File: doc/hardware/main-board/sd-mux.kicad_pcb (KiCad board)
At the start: 2 copper layers, 50 x 132 mm, 54 parts, among them J1 SDCARD, P1 USB_OTG, P10 MKDS 1,5/3, P2 629105136821, P3 61400416021, P4 61400416021, P5 IDC_02X04, P6 IDC_02X04, P7 MKDS 1,5/3, Q1 IRF7606PBF, Q2 IRF7606PBF, Q3 IRF7606PBF, Q4 IRF7606PBF, Q5 2N7002, Q6 2N7002, Q7 IRF7606PBF, Q8 IRF7606PBF, U1 TS3USB30EDGSR, U2 FT245RL, U3 74AHC1G14, U4 TS3A27518E, U5 74AHC1G14

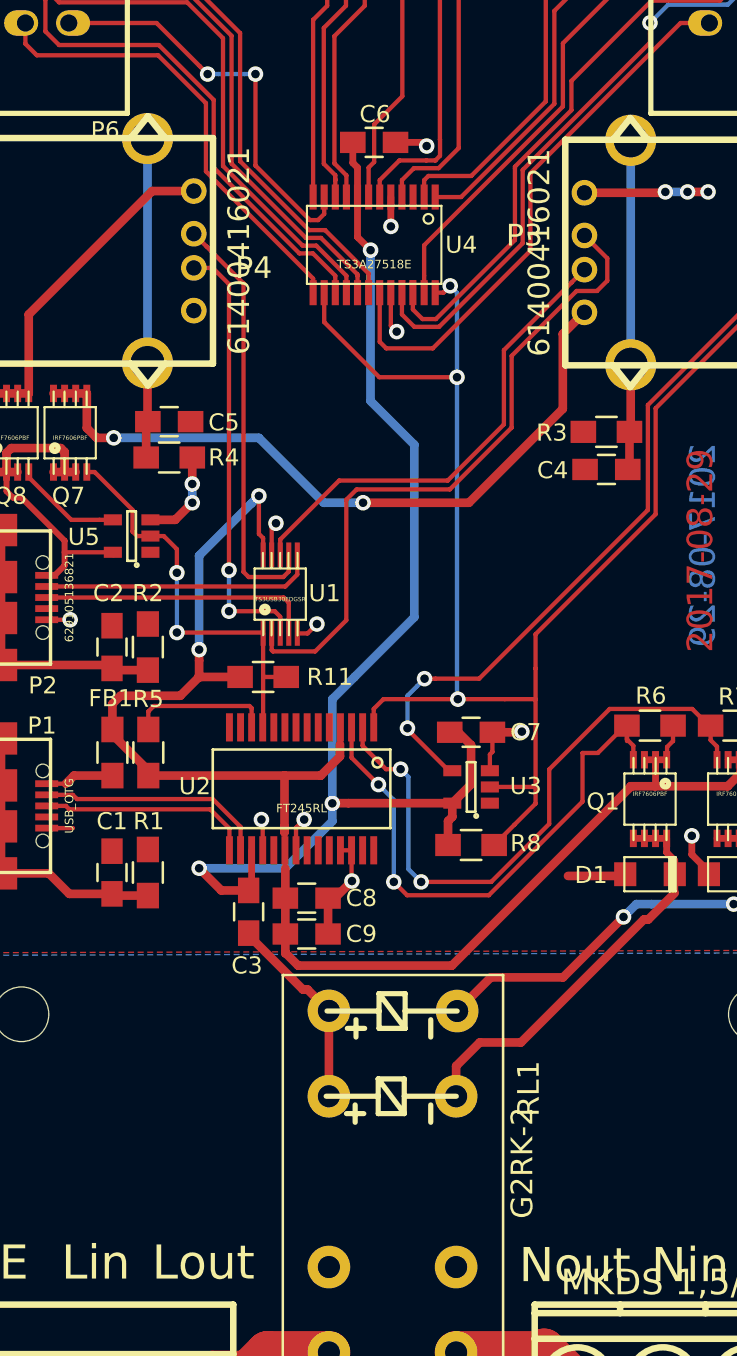
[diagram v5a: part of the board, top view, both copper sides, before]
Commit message: Fix unrouted tracks
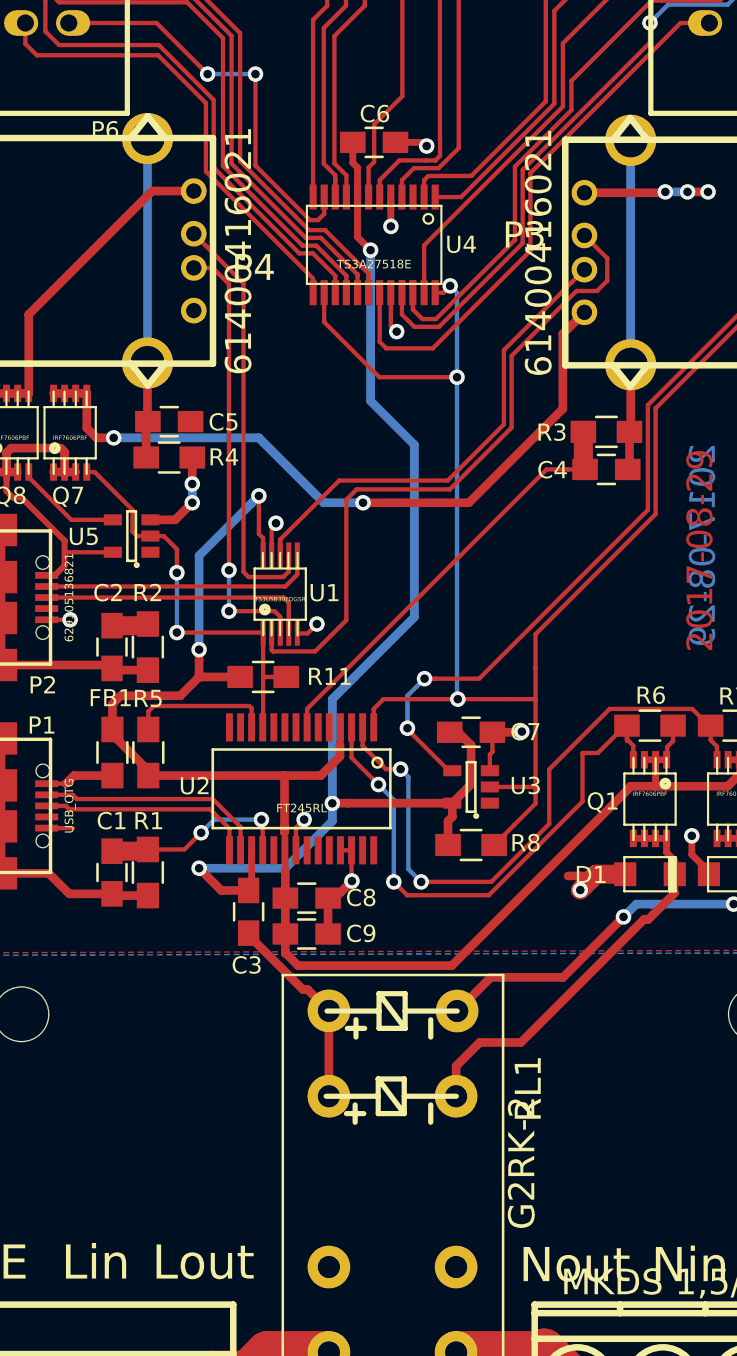
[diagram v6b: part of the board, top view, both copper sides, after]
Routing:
- net GND: track 157.1 -> 197.2 mm, vias 26 -> 28
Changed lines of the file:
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@@
-(kicad_pcb (version 4) (host pcbnew 4.0.5)
+(kicad_pcb (version 20171130) (host pcbnew "(5.0.0-rc2-dev-707-g2ed24a4)")
   (general
-    (links 171)
-    (no_connects 0)
-    (area 118.124519 15.525479 168.274521 147.675481)
     (thickness 1.6)
     (drawings 19)
-    (tracks 731)
+    (tracks 749)
     (zones 0)
     (modules 54)
@@
   )
   (setup
-    (last_trace_width 0.254)
+    (last_trace_width 1.116)
     (user_trace_width 0.508)
     (user_trace_width 1.116)
@@
       (layerselection 0x010fc_80000001)
       (usegerberextensions true)
+      (usegerberattributes false)
+      (usegerberadvancedattributes false)
+      (creategerberjobfile false)
       (excludeedgelayer false)
       (linewidth 0.100000)
@@
       (hpglpenspeed 20)
       (hpglpendiameter 15)
-      (hpglpenoverlay 2)
       (psnegative false)
       (psa4output false)
@@
     (tags SOT-23-5)
     (attr smd)
-    (fp_text reference U3 (at -3.2 0.05 360) (layer F.SilkS)
+    (fp_text reference U3 (at -3.2 0.05) (layer F.SilkS)
       (effects (font (size 1 1) (thickness 0.15)))
     )
@@
     (at 131.13626 43.545748 270)
     (descr MSOIC-8)
-    (fp_text reference Q3 (at 2.354732 -0.06326 360) (layer F.SilkS)
+    (fp_text reference Q3 (at 2.354732 -0.06326) (layer F.SilkS)
       (effects (font (size 1 1) (thickness 0.15)))
     )
@@
     (tags "capacitor 0805")
     (attr smd)
-    (fp_text reference C3 (at 3.15 0.1 360) (layer F.SilkS)
+    (fp_text reference C3 (at 3.15 0.1) (layer F.SilkS)
       (effects (font (size 1 1) (thickness 0.15)))
     )
@@
     (tags "capacitor 0805")
     (attr smd)
-    (fp_text reference C4 (at 3.15 -0.05 360) (layer F.SilkS)
+    (fp_text reference C4 (at 3.15 -0.05) (layer F.SilkS)
       (effects (font (size 1 1) (thickness 0.15)))
     )
@@
     (tags "resistor 0805")
     (attr smd)
-    (fp_text reference FB1 (at -3.17452 0.10548 360) (layer F.SilkS)
+    (fp_text reference FB1 (at -3.17452 0.10548) (layer F.SilkS)
       (effects (font (size 1 1) (thickness 0.15)))
     )
@@
     (at 120.45 99.85 270)
     (descr "USB B micro")
-    (fp_text reference P1 (at -4.7 -2.4 360) (layer F.SilkS)
+    (fp_text reference P1 (at -4.7 -2.4) (layer F.SilkS)
       (effects (font (size 1 1) (thickness 0.15)))
     )
@@
     (at 120.45 87.65 270)
     (descr "USB B micro")
-    (fp_text reference P2 (at 5.15048 -2.44952 360) (layer F.SilkS)
+    (fp_text reference P2 (at 5.15048 -2.44952) (layer F.SilkS)
       (effects (font (size 1 1) (thickness 0.15)))
     )
@@
     (at 159.19952 133.65048 180)
     (descr "3 Pins 5mm screw connector")
-    (fp_text reference P7 (at 0.2 -6.6 360) (layer F.SilkS)
+    (fp_text reference P7 (at 0.2 -6.6) (layer F.SilkS)
       (effects (font (size 1 1) (thickness 0.25)))
     )
@@
     (tags "resistor 0805")
     (attr smd)
-    (fp_text reference R3 (at 3.2 -0.05 360) (layer F.SilkS)
+    (fp_text reference R3 (at 3.2 -0.05) (layer F.SilkS)
       (effects (font (size 1 1) (thickness 0.15)))
     )
@@
     (descr "relay, V23042-B2 series")
     (fp_text reference RL1 (at -7.95 -7.95 270) (layer F.SilkS)
-      (effects (font (thickness 0.3048)))
+      (effects (font (size 1.524 1.524) (thickness 0.3048)))
     )
     (fp_text value G2RK-2 (at -3.6 -7.57 270) (layer F.SilkS)
-      (effects (font (thickness 0.3048)))
+      (effects (font (size 1.524 1.524) (thickness 0.3048)))
     )
     (fp_line (start 14.6 6.45) (end 14.6 -6.45) (layer F.SilkS) (width 0.15))
@@
     (descr "USB A Socket")
     (fp_text reference P3 (at 1 -9.5 180) (layer F.SilkS)
-      (effects (font (thickness 0.3048)))
+      (effects (font (size 1.524 1.524) (thickness 0.3048)))
     )
     (fp_text value 61400416021 (at 0 -8.636 90) (layer F.SilkS)
-      (effects (font (thickness 0.3048)))
+      (effects (font (size 1.524 1.524) (thickness 0.3048)))
     )
     (fp_line (start -7.62 6.985) (end 7.62 6.985) (layer F.SilkS) (width 0.381))
@@
     (at 125.75 67.35 270)
     (descr "USB A Socket")
-    (fp_text reference P4 (at 1 -9.5 360) (layer F.SilkS)
-      (effects (font (thickness 0.3048)))
+    (fp_text reference P4 (at 1 -9.5) (layer F.SilkS)
+      (effects (font (size 1.524 1.524) (thickness 0.3048)))
     )
     (fp_text value 61400416021 (at 0 -8.636 270) (layer F.SilkS)
-      (effects (font (thickness 0.3048)))
+      (effects (font (size 1.524 1.524) (thickness 0.3048)))
     )
     (fp_line (start -7.62 6.985) (end 7.62 6.985) (layer F.SilkS) (width 0.381))
@@
     (descr "PINS Box 4x2 2.54")
     (tags "CONN DEV")
-    (fp_text reference P6 (at 10.09952 -3.40048 360) (layer F.SilkS)
+    (fp_text reference P6 (at 10.09952 -3.40048) (layer F.SilkS)
       (effects (font (size 1 1) (thickness 0.2032)))
     )
@@
   (segment (start 123.12462 88.95048) (end 124.49952 88.95048) (width 0.254) (layer F.Cu) (net 2))
   (segment (start 124.49952 88.95048) (end 124.5 88.95) (width 0.254) (layer F.Cu) (net 2))
+  (segment (start 153.64504 80.15) (end 154.64904 80.15) (width 0.254) (layer F.Cu) (net 2))
+  (segment (start 152.39644 80.15) (end 153.64504 80.15) (width 0.254) (layer F.Cu) (net 2))
+  (segment (start 138.37512 94.17132) (end 152.39644 80.15) (width 0.254) (layer F.Cu) (net 2))
+  (segment (start 138.37512 95.25082) (end 138.37512 94.17132) (width 0.254) (layer F.Cu) (net 2))
+  (via (at 132.16952 101.42328) (size 0.91) (drill 0.5) (layers F.Cu B.Cu) (net 2))
+  (segment (start 131.1928 102.4) (end 132.16952 101.42328) (width 0.254) (layer F.Cu) (net 2))
+  (segment (start 129.05 102.4) (end 131.1928 102.4) (width 0.254) (layer F.Cu) (net 2))
+  (segment (start 132.94232 100.65048) (end 135.69952 100.65048) (width 0.254) (layer B.Cu) (net 2))
+  (segment (start 132.16952 101.42328) (end 132.94232 100.65048) (width 0.254) (layer B.Cu) (net 2))
+  (segment (start 128.95 102.5) (end 129.05 102.4) (width 1.116) (layer F.Cu) (net 2))
+  (segment (start 126.95 102.5) (end 128.95 102.5) (width 1.116) (layer F.Cu) (net 2))
+  (via (at 154.36912 104.77608) (size 0.91) (drill 0.5) (layers F.Cu B.Cu) (net 2))
+  (segment (start 155.2952 103.85) (end 154.36912 104.77608) (width 1.116) (layer F.Cu) (net 2))
+  (segment (start 156.99966 103.85) (end 155.2952 103.85) (width 1.116) (layer F.Cu) (net 2))
+  (segment (start 154.54904 80.05) (end 154.64904 80.15) (width 1.116) (layer F.Cu) (net 2))
+  (segment (start 154.54904 77.95) (end 154.54904 80.05) (width 1.116) (layer F.Cu) (net 2))
+  (segment (start 128.95 89.3) (end 129.05 89.2) (width 1.116) (layer F.Cu) (net 2))
+  (segment (start 126.95 89.3) (end 128.95 89.3) (width 1.116) (layer F.Cu) (net 2))
   (segment (start 120.45 83.7003) (end 120.45 86.45112) (width 0.508) (layer F.Cu) (net 3))
   (segment (start 120.45 86.45112) (end 120.45 88.84888) (width 0.508) (layer F.Cu) (net 3))

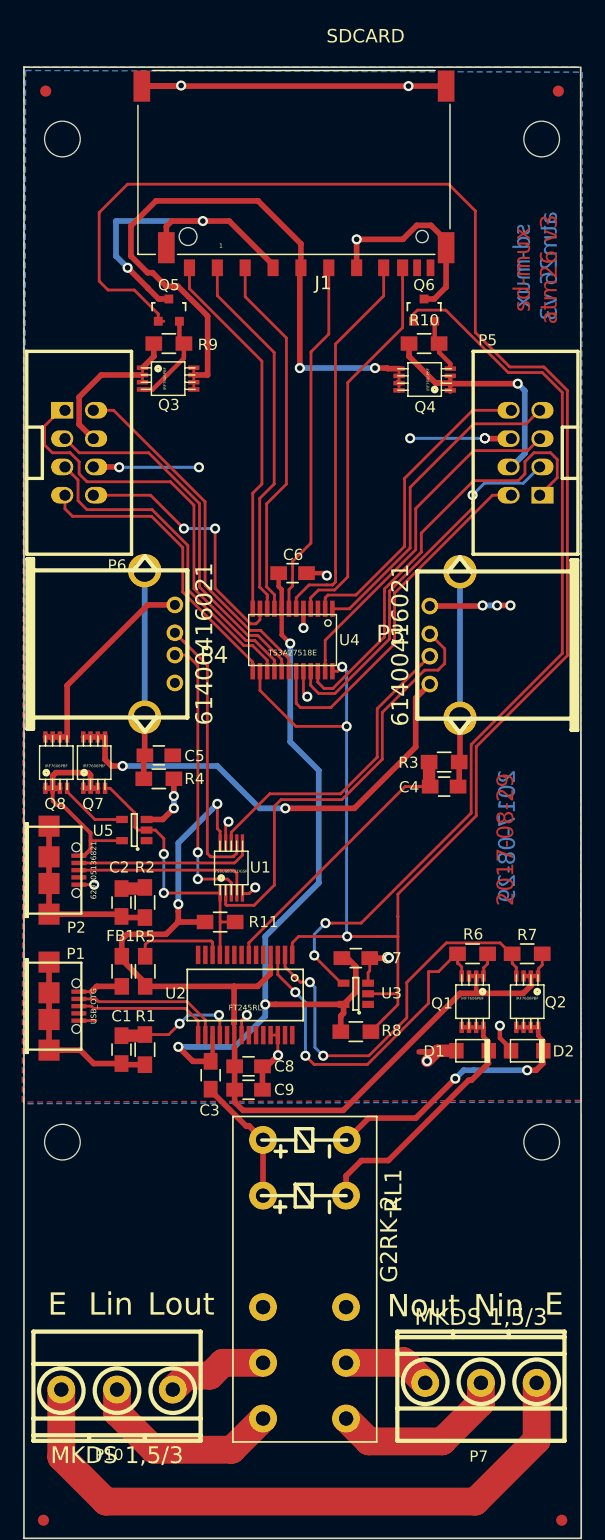
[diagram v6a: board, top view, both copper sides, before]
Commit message: Move 8w headers up so can fit shrouded 10w versions, flip so can use right angled
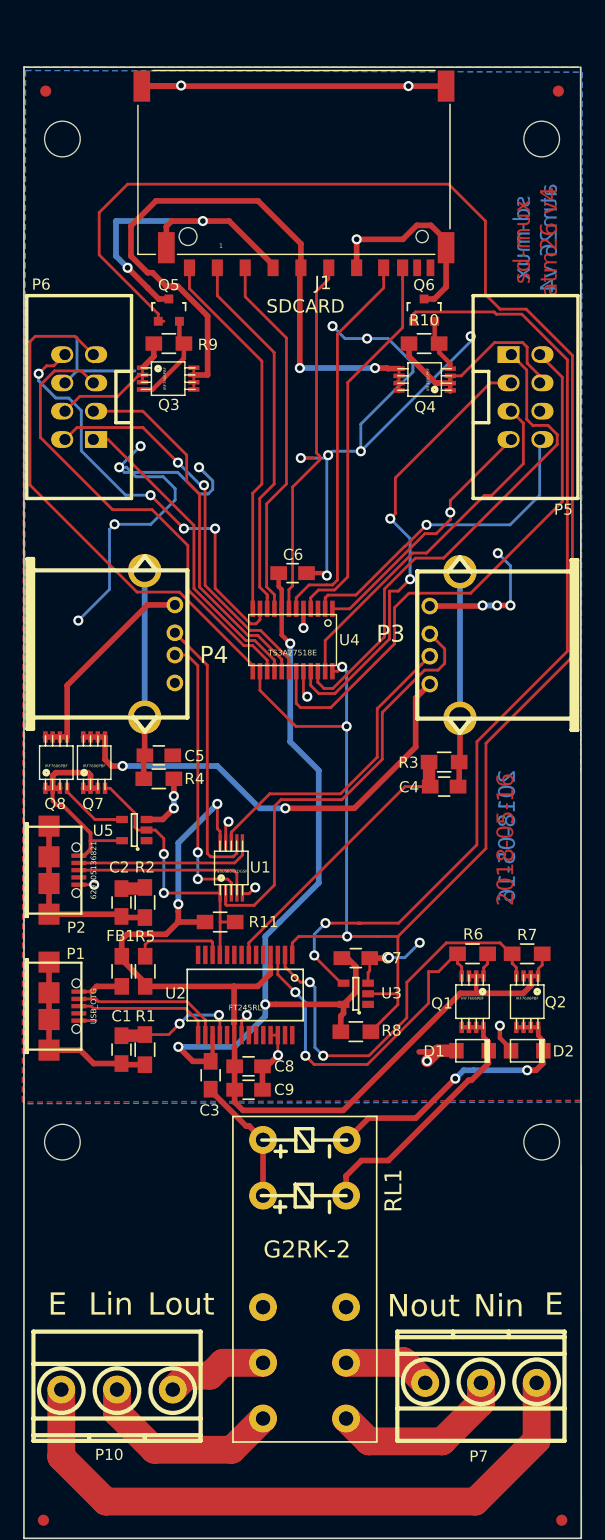
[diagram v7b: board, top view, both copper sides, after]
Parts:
- moved P5 5.00 mm to (163.2, 45.2), turned to 270 degrees
- moved P6 5.00 mm to (123.2, 45.2), turned to 90 degrees
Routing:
- net GND: track 197.2 -> 285.4 mm, vias 28 -> 36
- net /DAT0_TS: track 26.9 -> 47.3 mm
- net /DAT3_DUT: track 32.9 -> 50.5 mm
- net /DAT1_TS: track 24.1 -> 39.0 mm, vias 2 -> 4
- net /CLK_TS: track 29.7 -> 41.9 mm
- net /DAT2_TS: track 38.8 -> 28.8 mm
- net /CMD_DUT: track 34.1 -> 41.2 mm, vias 1 -> 2
- net /DAT0_DUT: track 29.3 -> 23.3 mm, vias 0 -> 1
- net /DAT2_DUT: track 39.7 -> 44.9 mm
- net Net-(Q6-Pad1): track 82.5 -> 87.0 mm
- net /DAT3_TS: track 32.3 -> 35.2 mm, vias 0 -> 2
- net /VDD_TS: track 14.7 -> 12.2 mm
- net /VDD_DUT: track 21.5 -> 19.1 mm, vias 1 -> 0
- net /DAT1_DUT: track 28.3 -> 29.8 mm, vias 0 -> 1
- net /SOCKET_SEL: track 185.6 -> 184.1 mm
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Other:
- board text added: "2018-05-16"
- board text added: "sd-mux atm26 v4"
- board text removed: "2017-08-29"
- board text removed: "sd-mux atm26 v3"

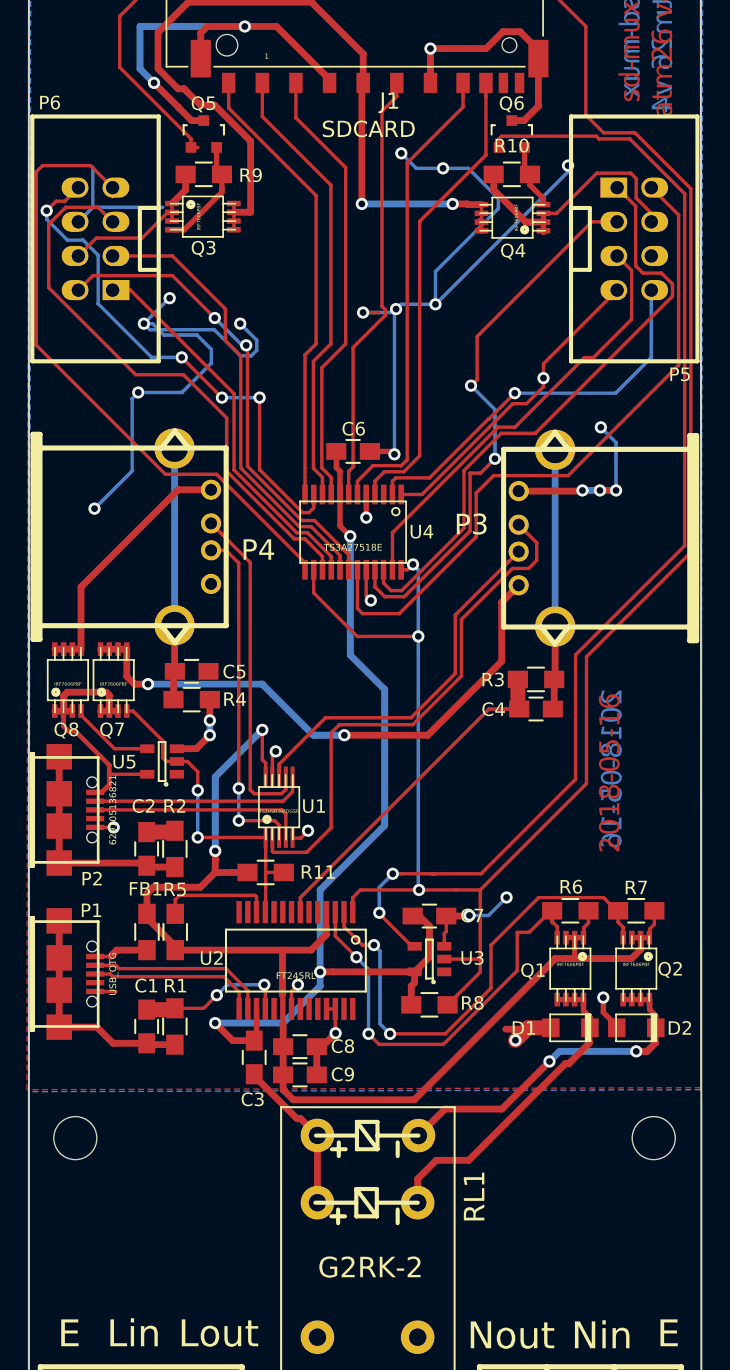
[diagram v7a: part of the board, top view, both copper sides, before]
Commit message: Fix up missing footprints, replace 8w IDC with 10w on PCB so can use common ribbon cables
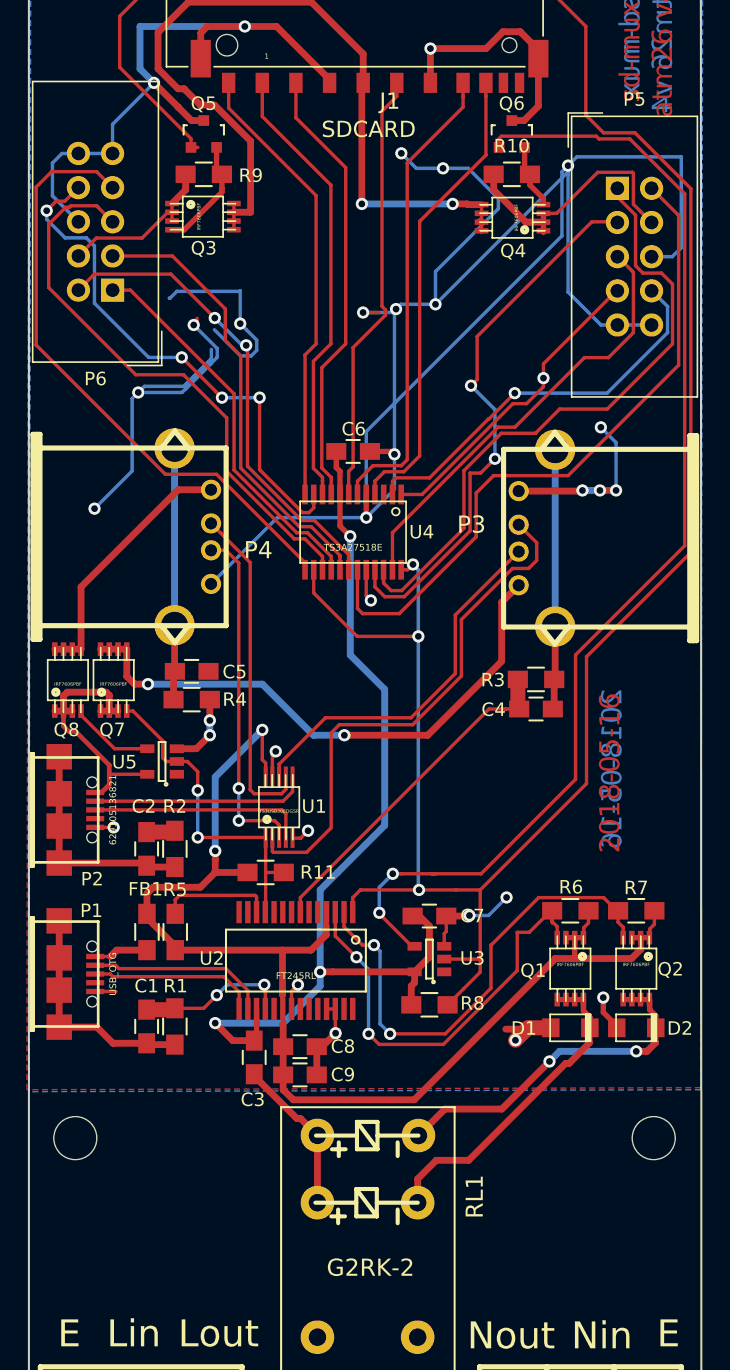
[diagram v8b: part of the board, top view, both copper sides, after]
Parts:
- P5, P6: value IDC_02X04 -> Conn_02x05_Odd_Even; footprint footprints:PSB_IDC_4x2 -> Connector_IDC:IDC-Header_2x05_P2.54mm_Vertical
- moved P6 4.02 mm to (124.4, 49.0), turned to 180 degrees
- moved P5 3.96 mm to (161.9, 41.4), turned to 0 degrees
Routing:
- net GND: track 285.4 -> 340.3 mm, vias 36 -> 31
- net (no net): track 0.00 -> 45.4 mm, vias 0 -> 4
- net /DAT2_DUT: track 44.9 -> 46.9 mm
- net /DAT0_TS: track 47.3 -> 46.3 mm
- net /VDD_DUT: track 19.1 -> 20.0 mm
- net /CLK_DUT: track 32.7 -> 33.4 mm
- net /DAT1_DUT: track 29.8 -> 30.5 mm
